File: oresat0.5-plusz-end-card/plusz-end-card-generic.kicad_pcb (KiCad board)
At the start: 4 copper layers, 99.8 x 94.6 mm, 28 parts, among them J2 Harwin M55-7101242R, J3 Harwin M55-7101242R, J4 Harwin M55-7101242R, J5 Harwin M55-7101242R

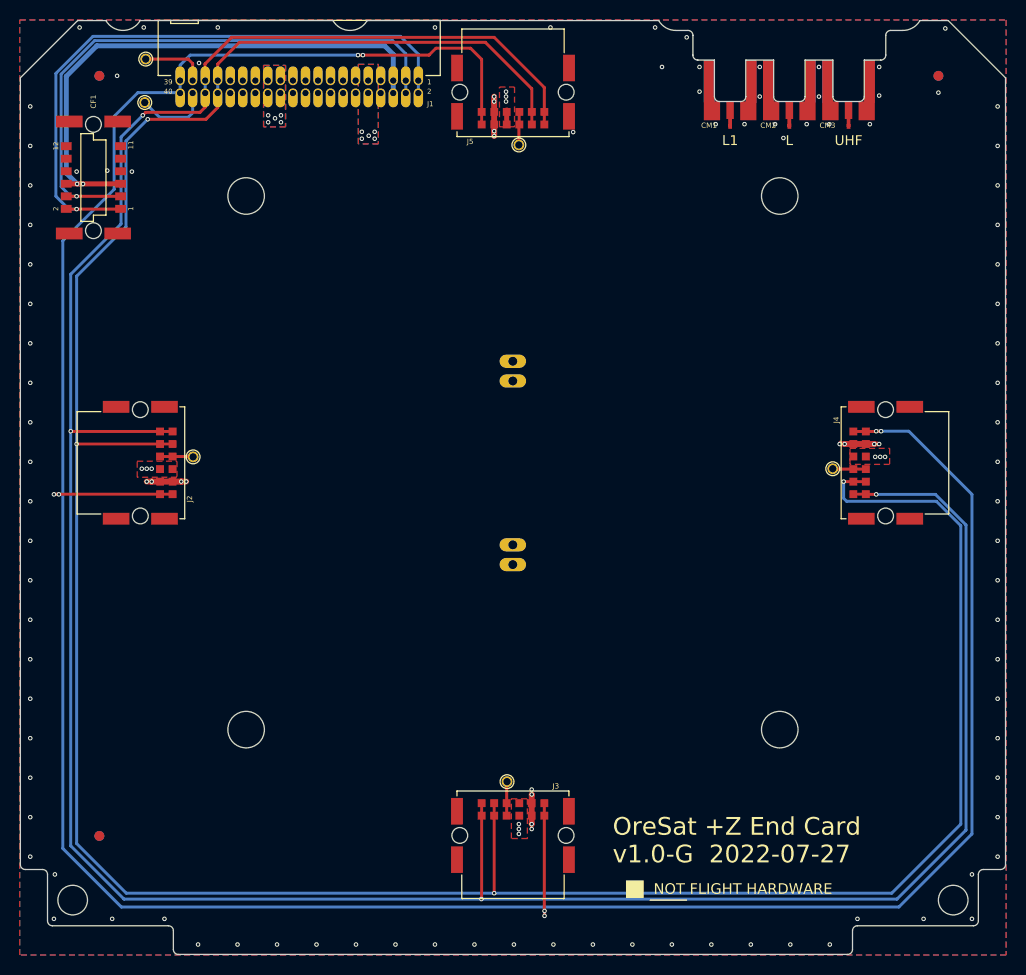
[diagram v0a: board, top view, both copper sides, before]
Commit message: First rev of OreSat0.5 +Z end card. Updated helical deployer, removed as much EAGLE cruft as easily possible, killed multiple sch sheets.
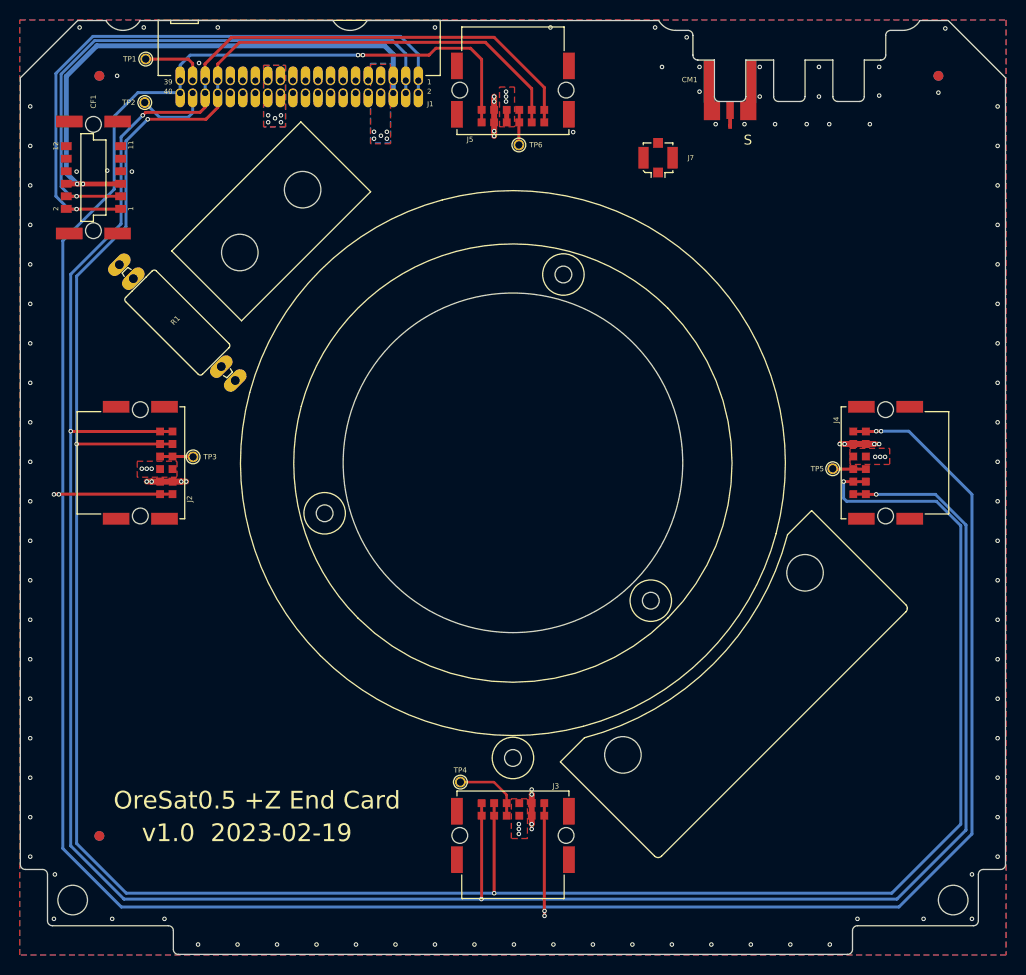
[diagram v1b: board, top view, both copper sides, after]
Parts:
- removed CM2, CM3: J-MOLEX-SMPM-73300-003X, oresat-footprints:J-MOLEX-SMPM-073300-003X
- removed U$1: FLIGHMARKERNEW, plusz-end-card-with-turnstile:FLIGHTMARKER_NEW_BOARDS
- added HW5: M1.6_Mounting_Hole, oresat-misc:M1.6 Mounting Hole, F.Cu at (129.4, 107.6)
- added HW6: M1.6_Mounting_Hole, oresat-misc:M1.6 Mounting Hole, F.Cu at (162.5, 116.5)
- added HW7: M1.6_Mounting_Hole, oresat-misc:M1.6 Mounting Hole, F.Cu at (148.5, 132.4)
- added HW8: M1.6_Mounting_Hole, oresat-misc:M1.6 Mounting Hole, F.Cu at (153.6, 83.4)
- added J7: U.FL2PIN, oresat-connectors:U.FL_Molex_MCRF_73412-0110_Vertical, F.Cu at (163.2, 71.6)
- CM1: footprint oresat-footprints:J-MOLEX-SMPM-073300-003X -> oresat-connectors:J-MOLEX-SMPM-073300-003X
- J1: value (none) -> J-SAMTEC-TFM-120-01-L-D-RA; footprint oresat-footprints:J-SAMTEC-TFM-120-X1-XXX-D-RA -> oresat-connectors:J-SAMTEC-TFM-120-X1-XXX-D-RA
- R1: footprint oresat-footprints:R-PAC100-FOR-MELTWIRE -> oresat-passives:R-PAC100-FOR-MELTWIRE; moved to F.Cu
- moved HW4 58.8 mm to (178.1, 113.6)
- moved HW1 48.3 mm to (127.2, 74.8)
- moved R1 36.8 mm to (114.5, 88.3), turned to 45 degrees
- moved HW2 16.1 mm to (159.6, 132.1)
- moved HW3 5.76 mm to (120.8, 81.2)
- moved TP4 4.73 mm to (143.2, 134.8), turned to 180 degrees
- moved J5 0.21 mm to (148.5, 64.8)
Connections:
- net /CONNECTORS/C3-UART-RX renamed /C3-UART-RX
- net /CONNECTORS/C3-UART-TX renamed /C3-UART-TX
- net /CONNECTORS/CAN1_H renamed /CAN1_H
- net /CONNECTORS/CAN1_L renamed /CAN1_L
- net /CONNECTORS/MAG-POWER renamed /MAG-POWER
- net /CONNECTORS/MAG-SCL renamed /MAG-SCL
- net /CONNECTORS/MAG-SDA renamed /MAG-SDA
- net /CONNECTORS/VBUS renamed VBUS
- net /CONNECTORS/~{SD} renamed /~{SD}
- net /L1 BAND/L1BAND renamed /S BAND
- J1 pad 10: /CONNECTORS/TURNSTILE-DEPLOY -> unconnected-(J1-Pad10)
- J1 pad 7: unconnected-(J1-Pad7) -> /HELICAL-DEPLOY
- J1 pad 8: unconnected-(J1-Pad8) -> /HELICAL-DEPLOY
- J1 pad 9: /CONNECTORS/TURNSTILE-DEPLOY -> unconnected-(J1-Pad9)
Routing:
- net Net-(J3-Pad7): track 3.49 -> 7.34 mm
- net GND: vias 112 -> 111
- net /HELICAL-DEPLOY: vias 0 -> 5
- net /CONNECTORS/TURNSTILE-DEPLOY: vias 5 -> 0
- added copper zone on B.Cu, net /HELICAL-DEPLOY
- added copper zone on F.Cu, net /HELICAL-DEPLOY
- added copper zone on In1.Cu, net /HELICAL-DEPLOY
- removed copper zone on B.Cu, net /CONNECTORS/TURNSTILE-DEPLOY
- removed copper zone on F.Cu, net /CONNECTORS/TURNSTILE-DEPLOY
- removed copper zone on In1.Cu, net /CONNECTORS/TURNSTILE-DEPLOY
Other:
- board text added: "OreSat0.5 +Z End Card"
- board text added: "S"
- board text added: "v1.0 2023-02-19"
- board text removed: "L"
- board text removed: "L1"
- board text removed: "OreSat +Z End Card"
- board text removed: "The exact position of this connector needs to be checked once we have the DXF"
- board text removed: "UHF"
- board text removed: "v1.0-G 2022-07-27"

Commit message: More KiCADing, new fiducials and footprints, fixed ERC and DRC. Now waiting on Cesar to do stuff.
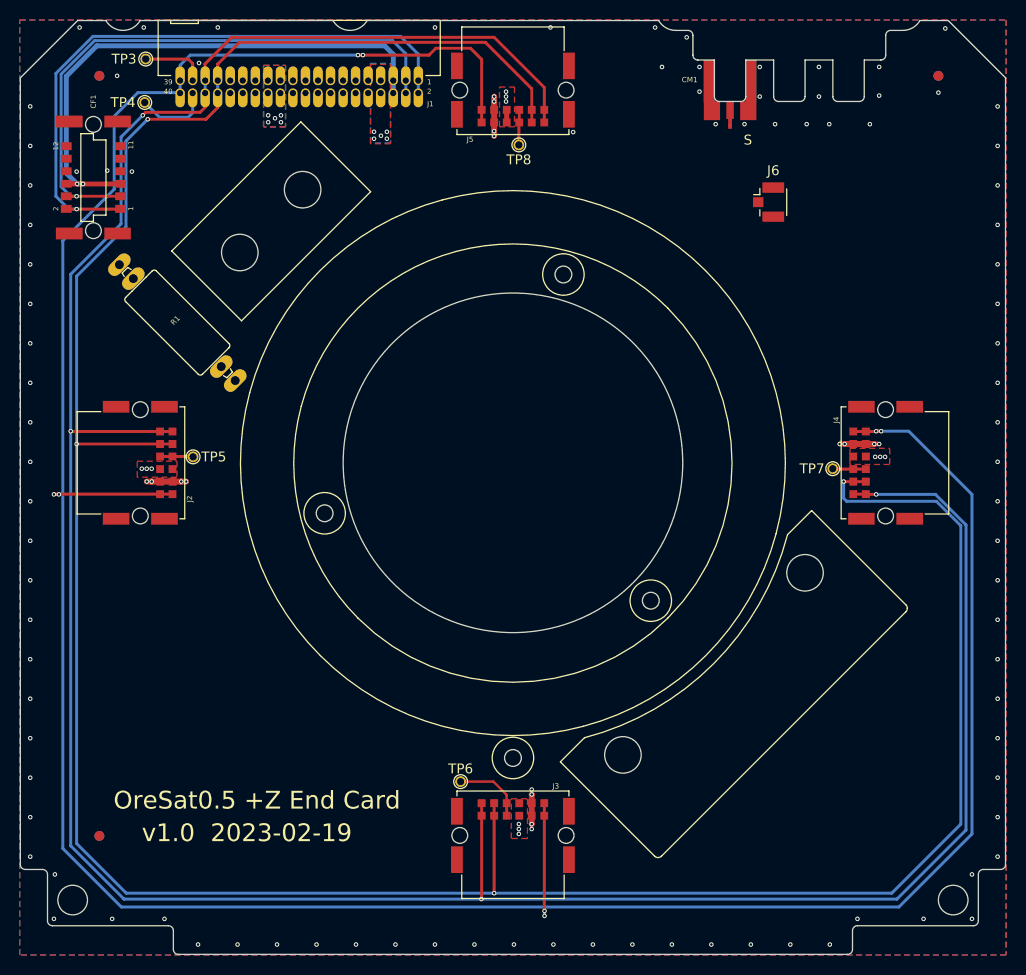
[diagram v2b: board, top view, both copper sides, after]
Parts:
- removed FIDUCIAL1, FIDUCIAL2, FIDUCIAL3, FIDUCIAL4, FIDUCIAL5, FIDUCIAL6: FIDUCIAL-1.0X2.0, plusz-end-card-with-turnstile:FIDUCIAL-1.0X2.0
- removed HW1, HW2, HW3, HW4: MCMASTER-94100A150, oresat-footprints:H-MCMASTER-94100A150
- removed J7: U.FL2PIN, oresat-connectors:U.FL_Molex_MCRF_73412-0110_Vertical
- removed TP1, TP2: TEST-POINT-LARGE-SQUARE, plusz-end-card-with-turnstile:1X01
- added FID1: Fiducial, Fiducial:Fiducial_1mm_Mask2mm, F.Cu at (106.6, 63.3)
- added FID2: Fiducial, Fiducial:Fiducial_1mm_Mask2mm, F.Cu at (191.6, 63.3)
- added FID3: Fiducial, Fiducial:Fiducial_1mm_Mask2mm, B.Cu at (191.6, 63.3)
- added FID4: Fiducial, Fiducial:Fiducial_1mm_Mask2mm, B.Cu at (106.6, 140.3)
- added FID5: Fiducial, Fiducial:Fiducial_1mm_Mask2mm, B.Cu at (106.6, 63.3)
- added FID6: Fiducial, Fiducial:Fiducial_1mm_Mask2mm, F.Cu at (106.6, 140.3)
- added HW10: M2-Press-Fit-Nut, oresat-misc:M2-Press-Fit-Nut, F.Cu at (159.6, 132.1)
- added HW11: M2-Press-Fit-Nut, oresat-misc:M2-Press-Fit-Nut, F.Cu at (178.1, 113.6)
- added HW12: M2-Press-Fit-Nut, oresat-misc:M2-Press-Fit-Nut, F.Cu at (127.2, 74.8)
- added HW9: M2-Press-Fit-Nut, oresat-misc:M2-Press-Fit-Nut, F.Cu at (120.8, 81.2)
- added J6: Conn_Coaxial, Connector_Coaxial:U.FL_Hirose_U.FL-R-SMT-1_Vertical, F.Cu at (174.4, 76.1)
- added TP7: TestPoint-MinTH, oresat-misc:TestPoint-MinTH, F.Cu at (180.9, 103.1)
- added TP8: TestPoint-MinTH, oresat-misc:TestPoint-MinTH, F.Cu at (149.1, 70.3)
- TP3, TP4, TP5, TP6: value TEST-POINT-LARGE-SQUARE -> TestPoint-MinTH; footprint plusz-end-card-with-turnstile:1X01 -> oresat-misc:TestPoint-MinTH
- moved TP4 75.9 mm to (111.2, 66.0), turned to 90 degrees
- moved TP5 64.8 mm to (116.1, 101.9), turned to -90 degrees
- moved TP6 64.8 mm to (143.2, 134.8), turned to 0 degrees
- moved TP3 40.6 mm to (111.3, 61.6)
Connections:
- TP3 pad 1: Net-(J2-Pad7) -> /C3-UART-TX
- TP4 pad 1: Net-(J3-Pad7) -> /C3-UART-RX
- TP5 pad 1: Net-(J4-Pad7) -> Net-(J2-Pad7)
- TP6 pad 1: Net-(J5-Pad7) -> Net-(J3-Pad7)
